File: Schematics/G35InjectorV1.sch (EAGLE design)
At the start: 11 parts

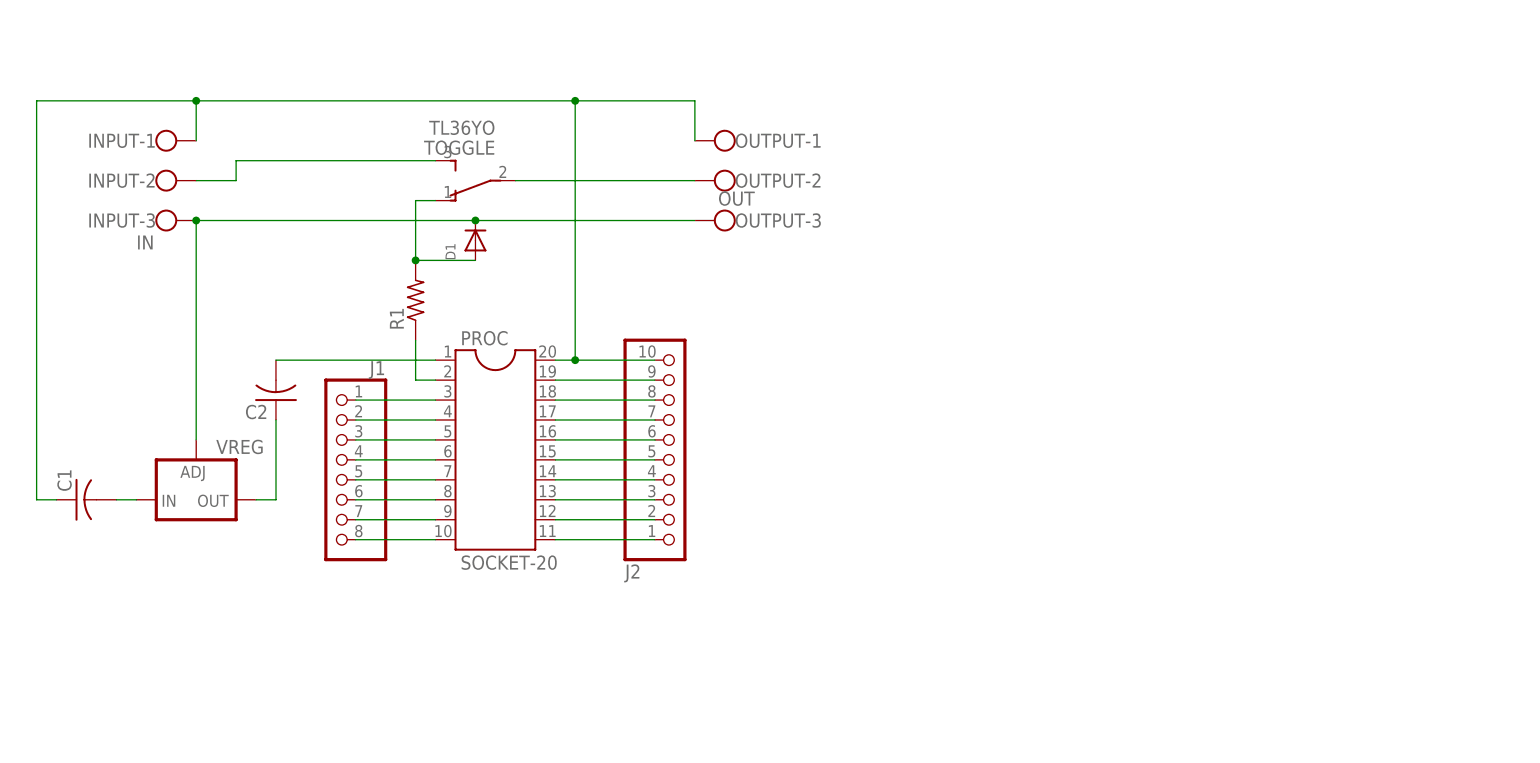
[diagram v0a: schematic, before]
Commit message: Fixed existing schematic
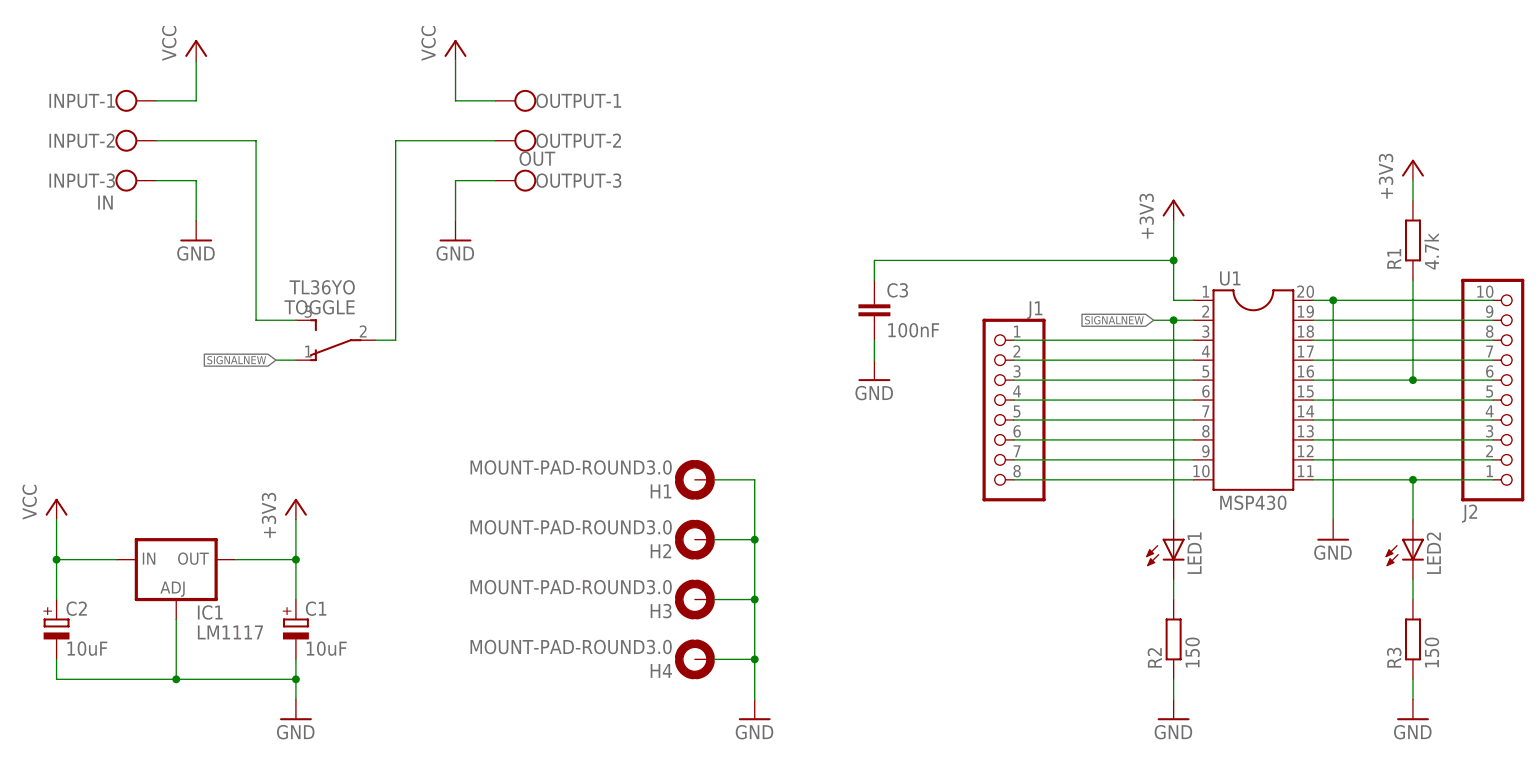
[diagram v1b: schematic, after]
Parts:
- removed D1: (no value), adafruit:DIODEDO-1N4148
- removed PROC: SOCKET-20, ic-package:DIL20S
- removed VREG: (no value), v-reg:LM138-TS
- added C3: 100nF, rcl:C-EUC0805
- added H1, H2, H3, H4: MOUNT-PAD-ROUND3.0, holes:MOUNT-PAD-ROUND3.0
- added IC1: LM1117, v-reg:LM317TS
- added LED1, LED2: (no value), led:LED5MM
- added R2, R3: 150, rcl:R-EU_R0805
- added U1: MSP430, ic-package:DIL20S
- C1, C2: value (none) -> 10uF; device adafruit:C-US050-045X075 -> rcl:CPOL-EUE5-10.5
- J1: device adafruit:PINHD-1X8BIG -> pinhead:PINHD-1X8
- R1: value (none) -> 4.7k; device adafruit:R-US_0207/9 -> rcl:R-EU_R0805
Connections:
- net SIGNALOUT renamed N$19
- removed net N$19 (its old number): C2.1, VREG.OUT
- removed net N$23: INPUT-2.KL
- removed net PVIN: C2.2, PROC.1
- removed net VIN: C1.1, INPUT-1.KL, J2.10, OUTPUT-1.KL, PROC.20
- new net +3V3: C1.+, C3.1, IC1.OUT, R1.2, U1.1
- new net N$20: LED1.C, R2.2
- new net N$21: LED2.C, R3.2
- new net VCC: C2.+, IC1.IN, INPUT-1.KL, OUTPUT-1.KL
- net GND: now also C1.-, C2.-, C3.2, H1.MOUNT, H2.MOUNT, H3.MOUNT, H4.MOUNT, IC1.ADJ, J2.10, R2.1, R3.1, U1.20; no longer D1.C, VREG.ADJ
- net N$1: now also U1.3; no longer PROC.3
- net N$10: now also U1.18; no longer PROC.18
- net N$11: now also U1.17; no longer PROC.17
- net N$12: now also R1.1, U1.16; no longer PROC.16
- net N$13: now also U1.15; no longer PROC.15
- net N$14: now also U1.14; no longer PROC.14
- net N$15: now also U1.13; no longer PROC.13
- net N$16: now also U1.12; no longer PROC.12
- net N$17: now also LED2.A, U1.11; no longer PROC.11
- net N$18: now also INPUT-2.KL, TOGGLE.S; no longer C1.2, VREG.IN
- net N$2: now also U1.4; no longer PROC.4
- net N$3: now also U1.5; no longer PROC.5
- net N$4: now also U1.6; no longer PROC.6
- net N$5: now also U1.7; no longer PROC.7
- net N$6: now also U1.8; no longer PROC.8
- net N$7: now also U1.9; no longer PROC.9
- net N$8: now also U1.10; no longer PROC.10
- net N$9: now also U1.19; no longer PROC.19
- net SIGNALNEW: now also LED1.A, U1.2; no longer D1.A, PROC.2, R1.1, R1.2
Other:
- moved on the sheet: INPUT-1, INPUT-2, INPUT-3, J2, OUTPUT-1, OUTPUT-2, OUTPUT-3, TOGGLE
